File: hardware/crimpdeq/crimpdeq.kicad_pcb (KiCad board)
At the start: 2 copper layers, 23 x 63.8 mm, 52 parts, among them J2 USB4105-GF-A, Q1 S8550, Q2 DMG3415U, SW1 SW_Push, SW2 SW_Push, U1 ESP32-C3-MINI-1, U2 MCP73831T-2ACI/OT, U3 HX711, U4 Rust_Board, U6 SY8088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

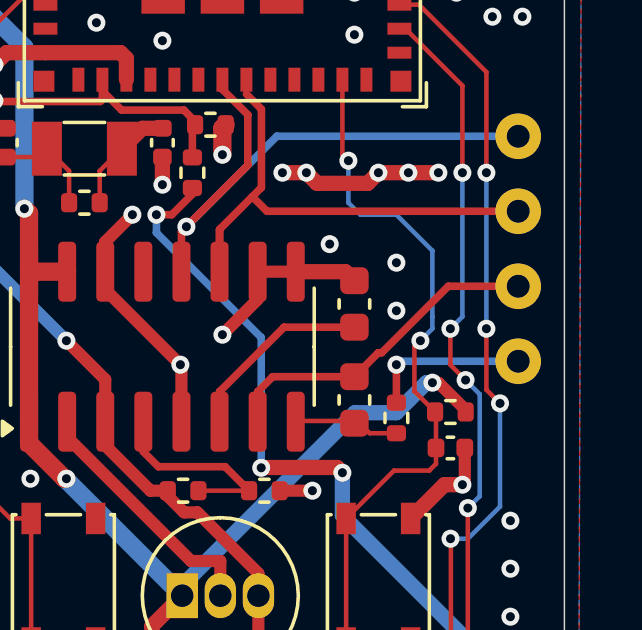
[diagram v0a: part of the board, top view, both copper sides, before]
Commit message: Update hx711 schematic according to the datasheet (#35)
* pcb: Update hx711 schematic according to the datasheet

* feat: Generate gerber files

* feat: Regenerate production files
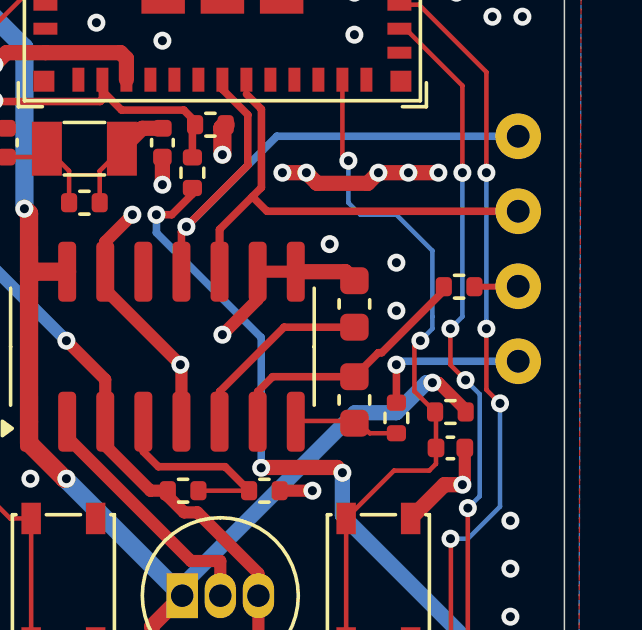
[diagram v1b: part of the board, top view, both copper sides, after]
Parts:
- added R8: 100R 1%, Resistor_SMD:R_0402_1005Metric, F.Cu at (148.7, 70.2)
- C10, C9: value 1uF -> 10uF
- C11: value 1uF -> 0.1uF
- R5: value 20kR 1% -> 12kR 1%
- R7: value 1kR 1% -> 100R 1%
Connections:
- C12 pad 2: A- -> Net-(U3-INA-)
- U3 pad 7: A- -> Net-(U3-INA-)
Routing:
- net A-: track 11.1 -> 1.47 mm
- net Net-(U3-INA-): track 0.00 -> 8.73 mm
